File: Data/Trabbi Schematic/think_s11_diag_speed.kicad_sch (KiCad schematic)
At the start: 5 parts, among them J1 Diagnostic Connector (C09), J2 Multi-connector D01/D02/D03, K1 Charge Cooling Relay R4, U1 Collision Sensor (C050), U2 Speed Signal

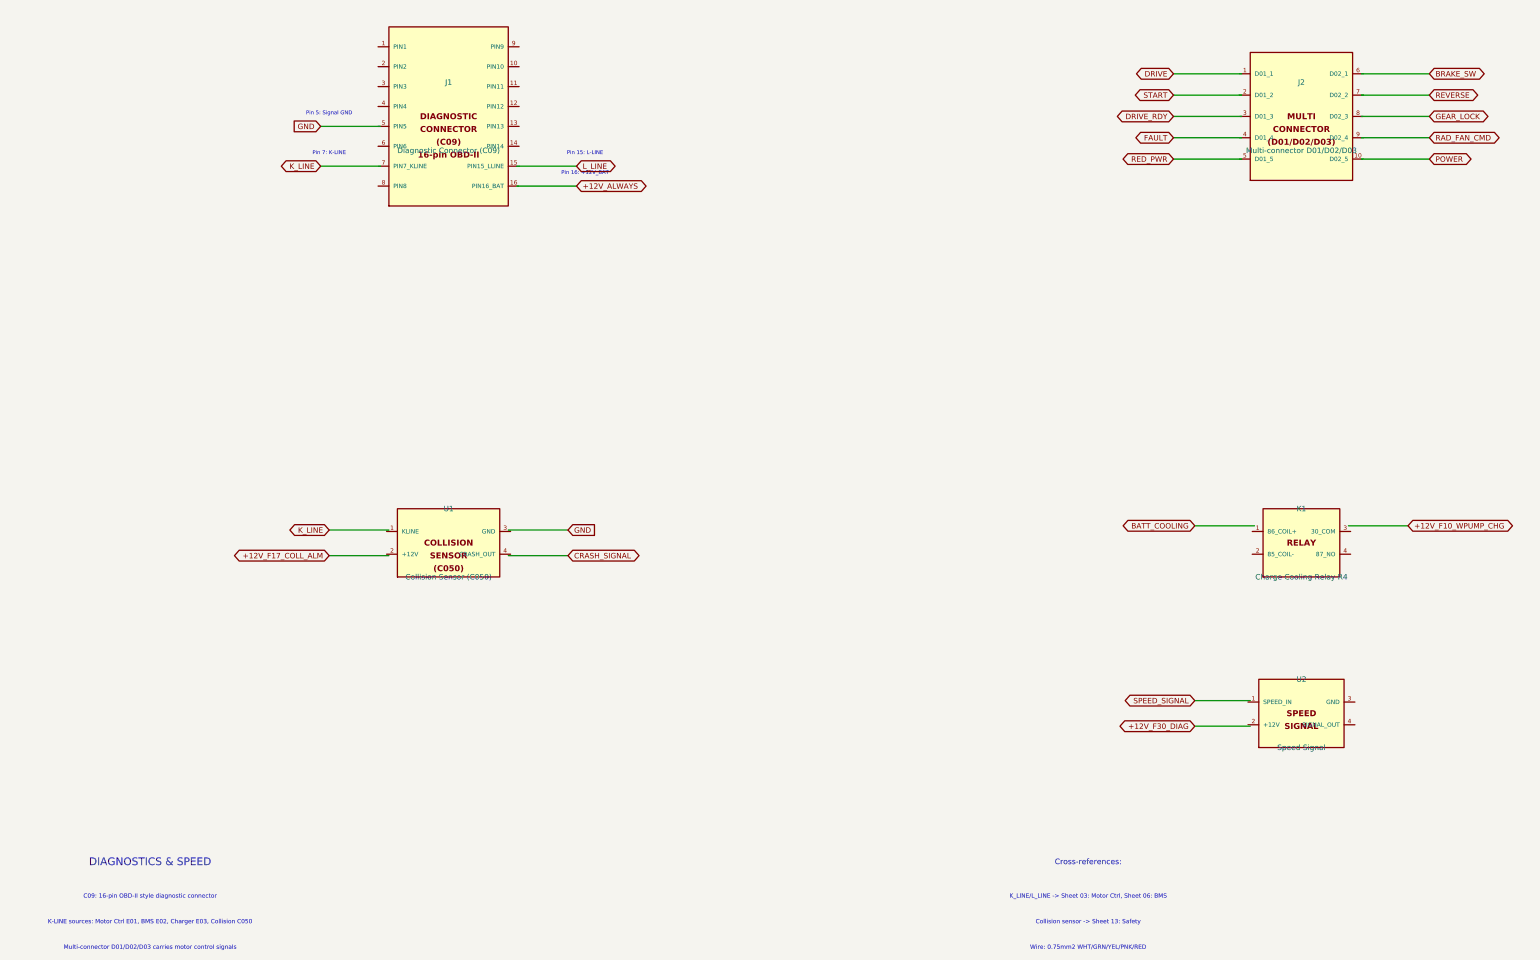
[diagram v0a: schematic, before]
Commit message: Fix wire-to-pin connections: use exact calculated pin positions
Refactored gen_think_complete.py to compute exact pin schematic
coordinates instead of using approximate manual offsets. Added p()
method to Sheet class that transforms symbol-local pin positions to
schematic coordinates. All 232 wire calls across 13 sub-sheet
generators now use p() for pin endpoints, fixing misaligned
connections (previously off by 0.54-10+ units).

Co-Authored-By: Claude Opus 4.6 <noreply@anthropic.com>
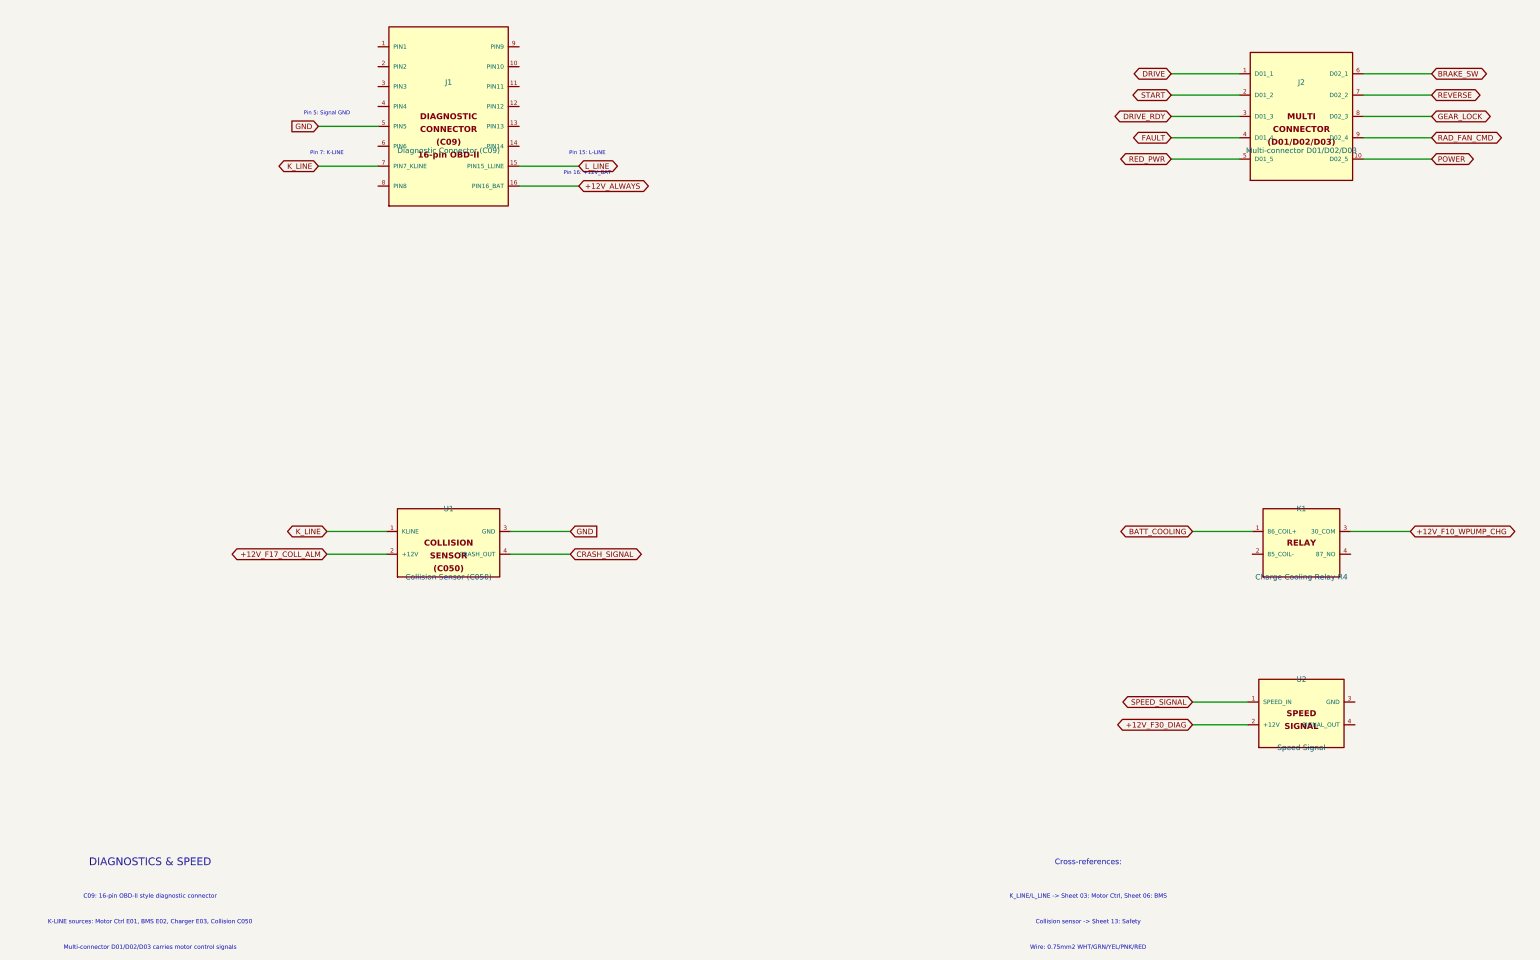
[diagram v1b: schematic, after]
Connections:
- net +12V_ALWAYS: now also J1.16 (PIN16_BAT)
- net +12V_F10_WPUMP_CHG: now also K1.3 (30_COM)
- net +12V_F17_COLL_ALM: now also U1.2 (+12V)
- net +12V_F30_DIAG: now also U2.2 (+12V)
- net BATT_COOLING: now also K1.1 (86_COIL+)
- net BRAKE_SW: now also J2.6 (D02_1)
- net CRASH_SIGNAL: now also U1.4 (CRASH_OUT)
- net DRIVE: now also J2.1 (D01_1)
- net DRIVE_RDY: now also J2.3 (D01_3)
- net FAULT: now also J2.4 (D01_4)
- net GEAR_LOCK: now also J2.8 (D02_3)
- net GND: now also J1.5 (PIN5), U1.3 (GND)
- net K_LINE: now also J1.7 (PIN7_KLINE), U1.1 (KLINE)
- net L_LINE: now also J1.15 (PIN15_LLINE)
- net POWER: now also J2.10 (D02_5)
- net RAD_FAN_CMD: now also J2.9 (D02_4)
- net RED_PWR: now also J2.5 (D01_5)
- net REVERSE: now also J2.7 (D02_2)
- net SPEED_SIGNAL: now also U2.1 (SPEED_IN)
- net START: now also J2.2 (D01_2)

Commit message: Enforce orthogonal routing and 1.27mm grid alignment
- Add _g() grid snap function to Sheet class (rounds all coordinates to nearest 1.27mm)
- Add wire_l() method for L-shaped orthogonal routing (horizontal+vertical segments)
- Apply grid snapping in p(), place(), wire(), label(), glabel(), junction(), no_connect(), defsym()
- Replace all 19 diagonal wire calls with wire_l() across S02, S06, S07, S08, S10, S12, S13
- All wire segments now strictly horizontal or vertical, no diagonals
- All coordinates verified on 1.27mm (50mil) KiCad standard grid

Co-Authored-By: Claude Opus 4.6 <noreply@anthropic.com>
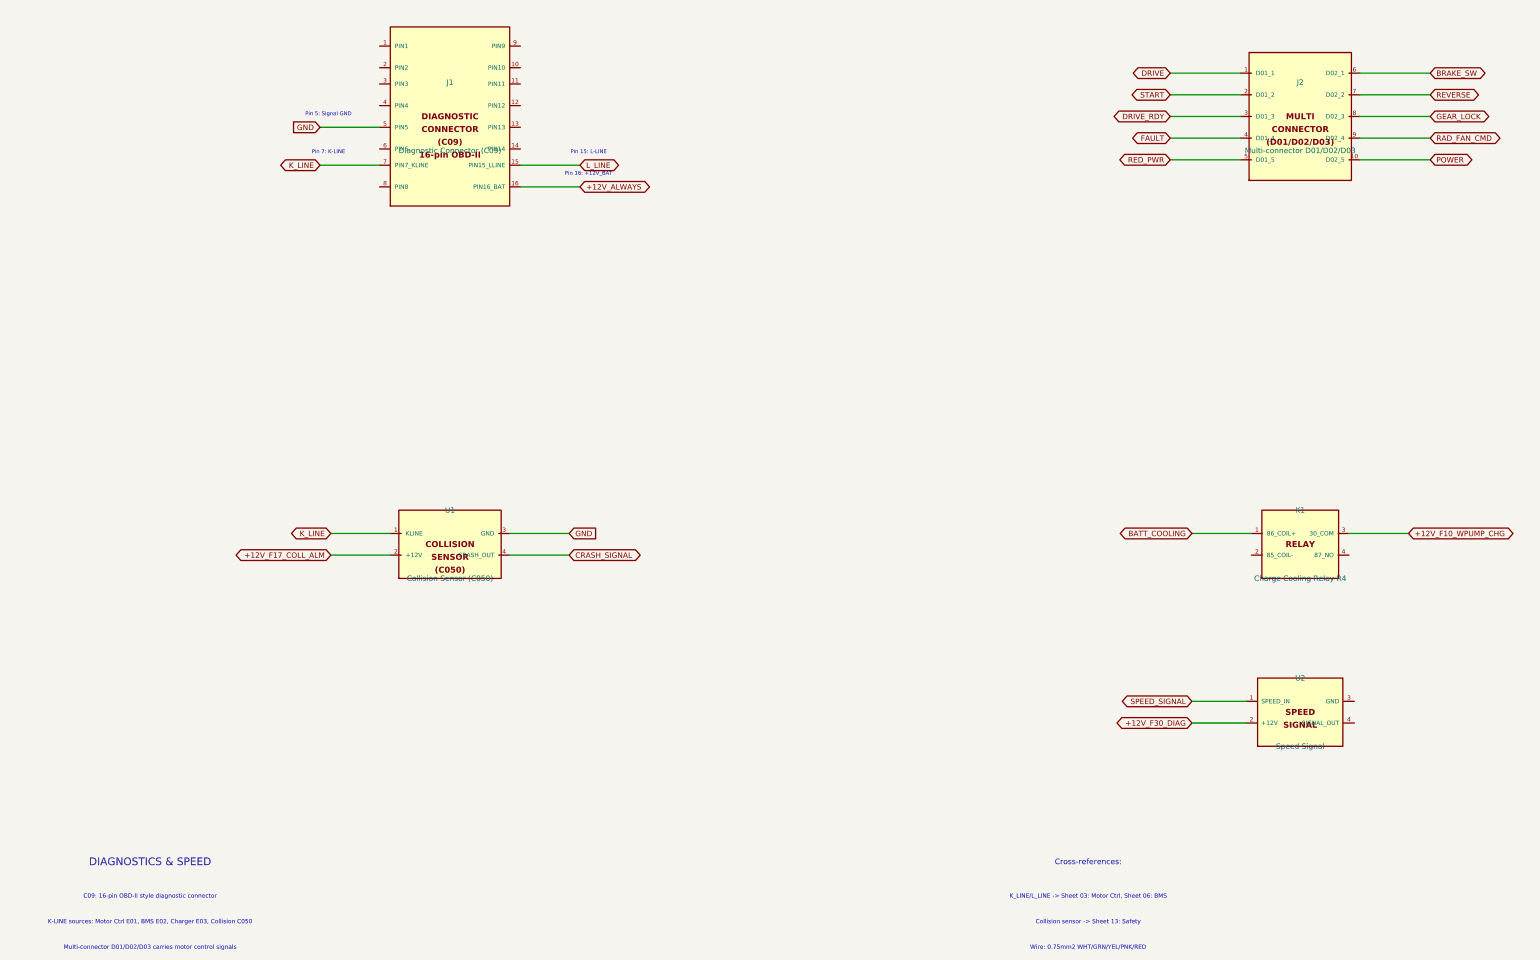
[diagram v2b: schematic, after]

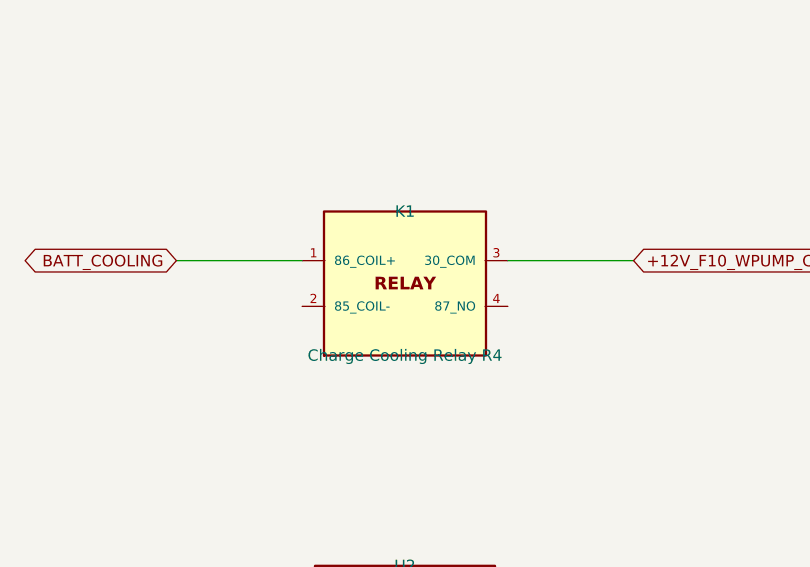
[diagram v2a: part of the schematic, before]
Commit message: Add relay coil/switch graphics, fix label positioning
- Draw coil (inductor arcs) and switch contacts (circles + arm)
  inside RELAY_SPST and RELAY_SPDT symbol bodies
- Add body_gfx parameter to defsym() for custom symbol graphics
- Helper functions: _gfx_polyline, _gfx_arc, _gfx_circle, _relay_gfx
- Fix label offsets: increase from 3-5mm to 10-12mm to avoid
  overlapping pin names (S01 ignition, S02 HV, S05 DCDC, S07 lights)
- Fix S09 turn signal rear labels: add wire stubs (were at 0 offset)
- All 14 schematics regenerated, parentheses balanced, grid OK

Co-Authored-By: Claude Opus 4.6 <noreply@anthropic.com>
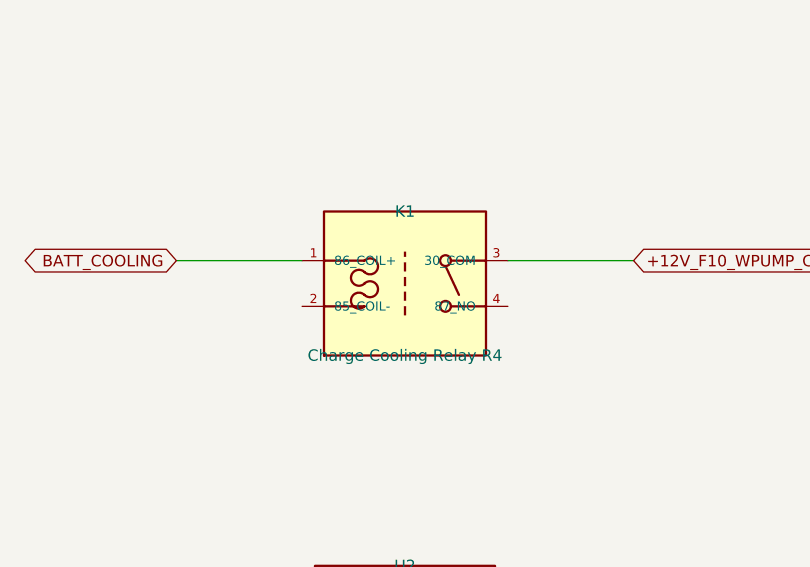
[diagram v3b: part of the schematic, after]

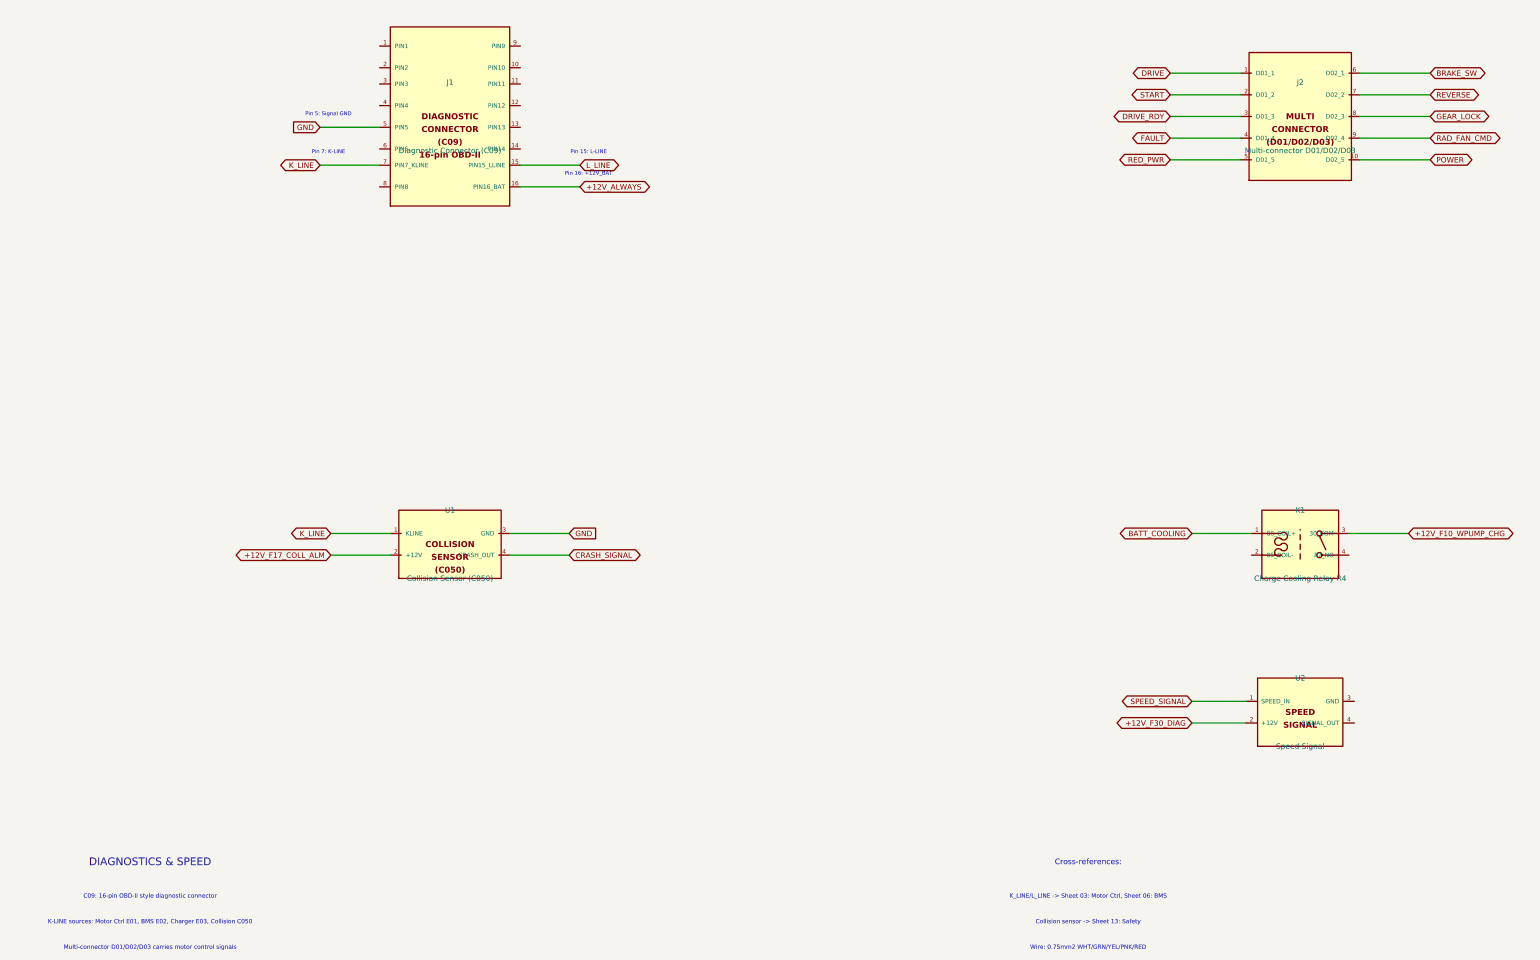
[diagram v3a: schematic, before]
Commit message: Fix label/text positioning: Ref/Value outside body, hide pin numbers
- Reference placed above body edge, Value below (dynamic based on
  symbol height) — no longer overlapping body text
- Pin numbers hidden (clutter, not useful in schematic view)
- Pin name font reduced from 1.016mm to 0.762mm (less overlap)
- Pin length increased from 2.54mm to 3.81mm (more room for pin names
  between body edge and endpoint)
- Store symbol dimensions in _sym_dims for dynamic property placement

Co-Authored-By: Claude Opus 4.6 <noreply@anthropic.com>
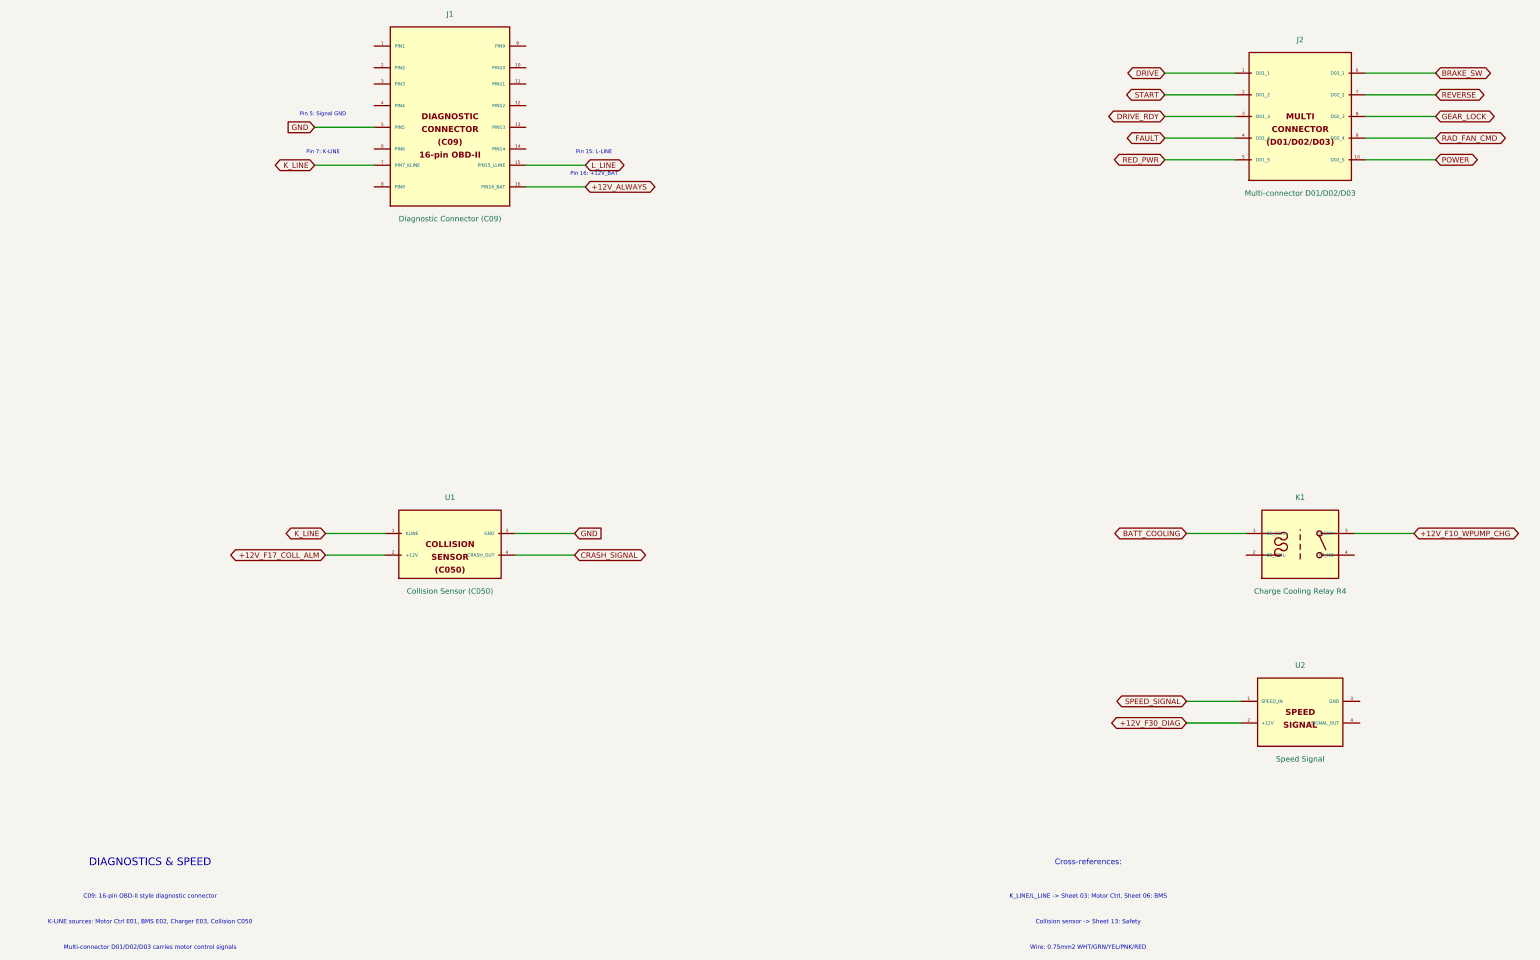
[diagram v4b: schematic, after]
